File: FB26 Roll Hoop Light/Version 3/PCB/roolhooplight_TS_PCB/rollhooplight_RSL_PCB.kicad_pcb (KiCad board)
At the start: 2 copper layers, 31.5 x 18.5 mm, 11 parts, among them J1 Conn_01x01, J2 Conn_01x01, J3 Conn_01x01, J4 Conn_01x01

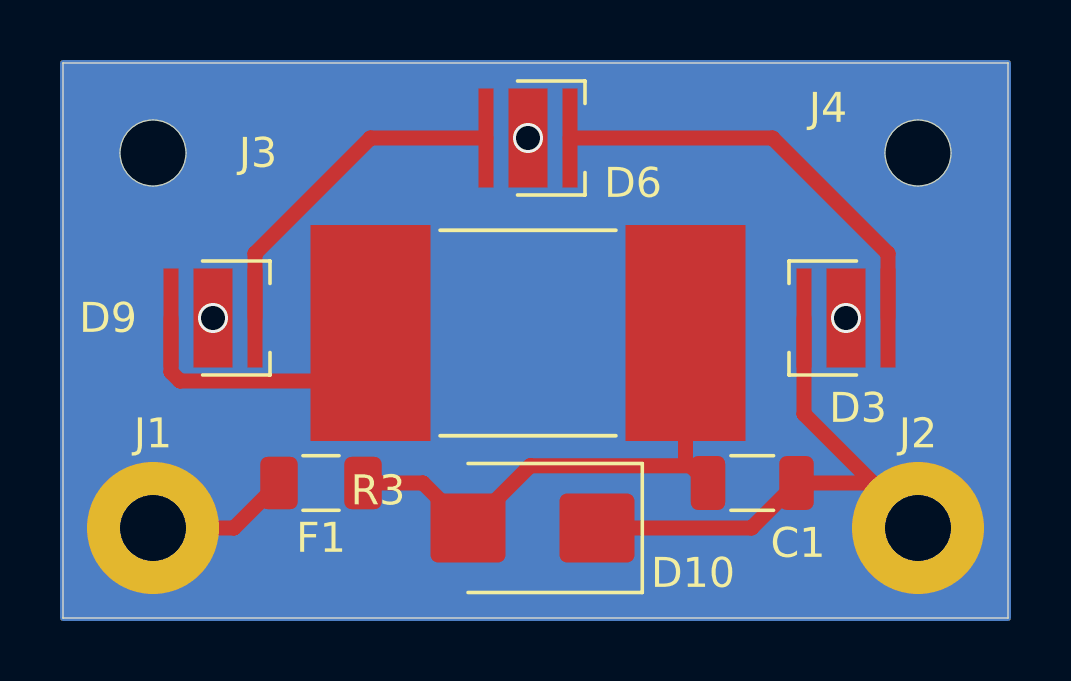
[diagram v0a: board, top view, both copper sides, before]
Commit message: fixed shorting issue*
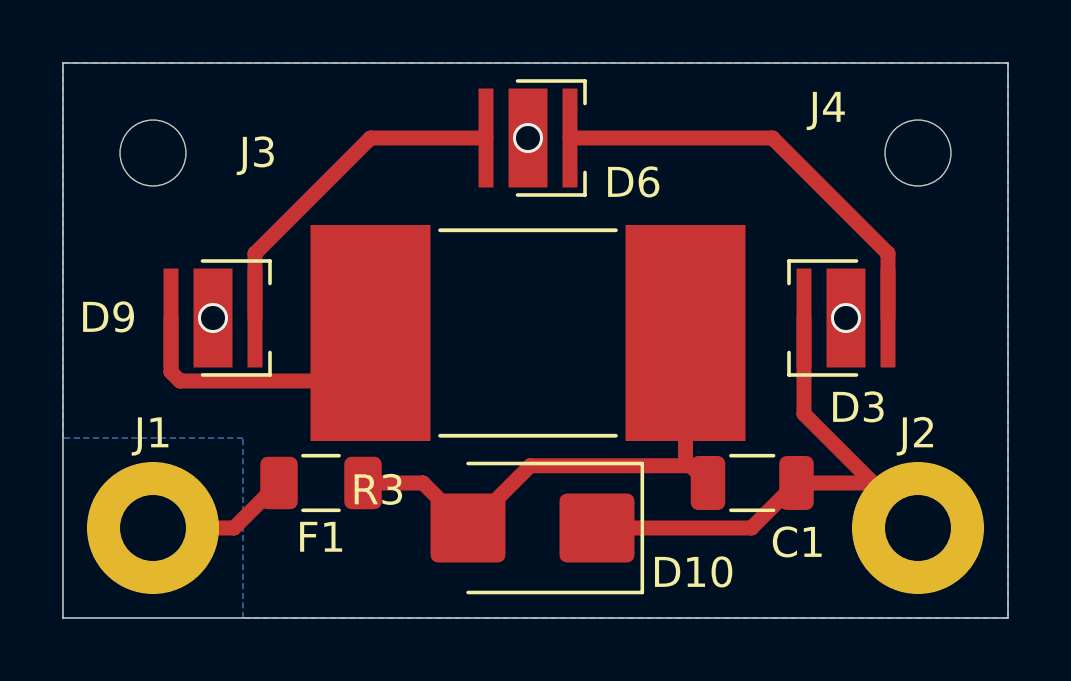
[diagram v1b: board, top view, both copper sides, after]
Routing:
- added copper zone on B.Cu, net GND
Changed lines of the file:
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@@
 			(size 4.4 4.4)
 			(drill 2.2)
-			(layers "*.Cu" "*.Mask")
-			(remove_unused_layers no)
+			(layers "*.Cu" "F.Mask")
+			(remove_unused_layers yes)
+			(keep_end_layers no)
+			(zone_layer_connections)
 			(net "+12V")
 			(pinfunction "Pin_1_1")
 			(pintype "passive")
+			(clearance 1)
 			(zone_connect 2)
 		)
@@
 		(end 111.5 60.5)
 		(stroke
-			(width 0.2)
-			(type solid)
-		)
-		(fill yes)
-		(layer "B.Cu")
-		(net "GND")
-	)
-	(gr_rect
-		(start 80 42)
-		(end 111.5 60.5)
-		(stroke
 			(width 0.05)
 			(type default)
@@
 		(net "+12V")
 	)
+	(zone
+		(net "GND")
+		(layer "B.Cu")
+		(hatch edge 0.5)
+		(connect_pads
+			(clearance 0.5)
+		)
+		(min_thickness 0.25)
+		(fill yes
+			(thermal_gap 0.5)
+			(thermal_bridge_width 0.5)
+			(island_removal_mode 0)
+		)
+		(polygon
+			(pts
+				(xy 80 42) (xy 111.5 42) (xy 111.5 60.5) (xy 86 60.5) (xy 86 54.5) (xy 80 54.5)
+			)
+		)
+	)
 	(embedded_fonts no)
